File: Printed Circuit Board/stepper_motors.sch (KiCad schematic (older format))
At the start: 8 parts, among them J7 Conn_01x04_Male, J8 Conn_01x04_Male

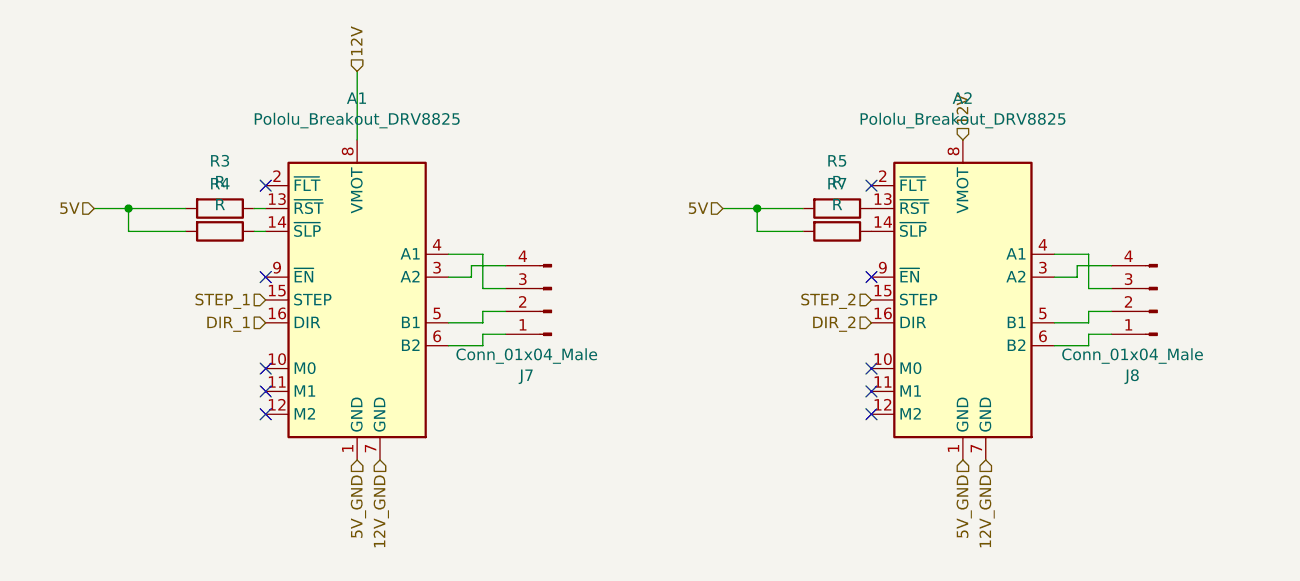
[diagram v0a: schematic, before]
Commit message: PCB: using m0, m1, m2 in stepper motors
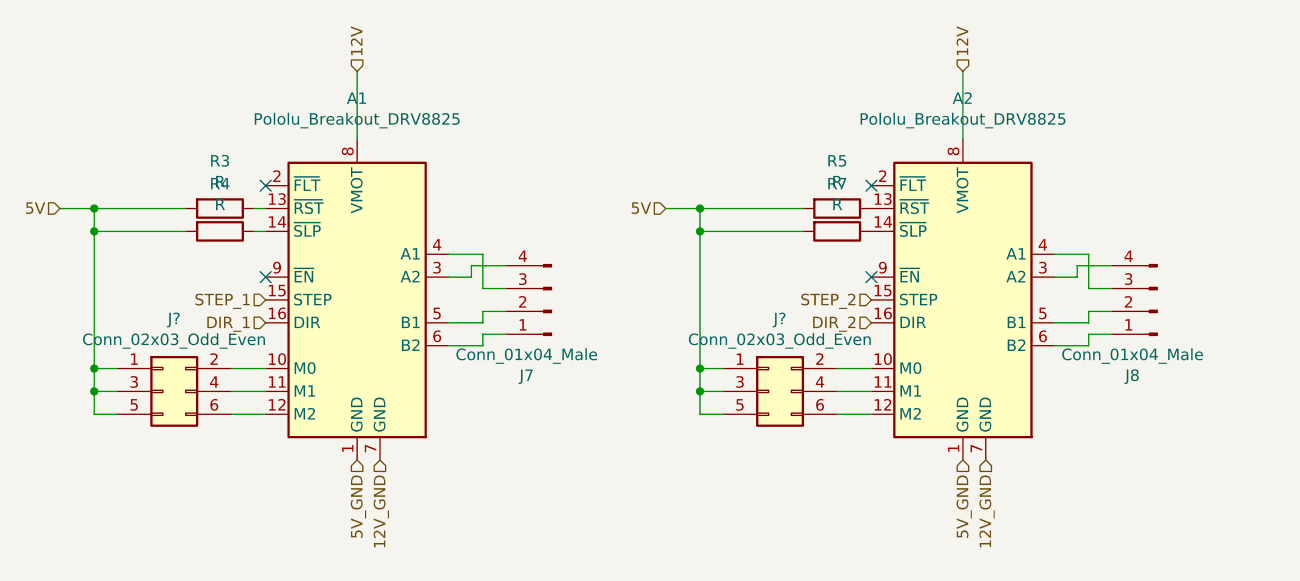
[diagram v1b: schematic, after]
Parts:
- added J? (x2): Conn_02x03_Odd_Even, symbol Connector_Generic:Conn_02x03_Odd_Even
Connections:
- net 5V: now also J?.1 (Pin_1), J?.1 (Pin_1), J?.3 (Pin_3), J?.3 (Pin_3), J?.5 (Pin_5), J?.5 (Pin_5)
- net at A1.10 (M0): now also J?.2 (Pin_2)
- net at A1.11 (M1): now also J?.4 (Pin_4)
- net at A1.12 (M2): now also J?.6 (Pin_6)
- net at A2.10 (M0): now also J?.2 (Pin_2)
- net at A2.11 (M1): now also J?.4 (Pin_4)
- net at A2.12 (M2): now also J?.6 (Pin_6)
- no-connect marks 10 -> 4
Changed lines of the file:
@@
 NoConn ~ 4300 4250
 NoConn ~ 6950 4250
-NoConn ~ 4300 4850
-NoConn ~ 4300 4750
-NoConn ~ 4300 4650
-NoConn ~ 6950 4850
-NoConn ~ 6950 4750
-NoConn ~ 6950 4650
 NoConn ~ 4300 3850
 NoConn ~ 6950 3850
@@
 $Comp
 L Driver_Motor:Pololu_Breakout_DRV8825 A?
-U 1 1 603C24B3
-P 4700 4250
-AR Path="/603C24B3" Ref="A?"  Part="1"
-AR Path="/603B418F/603C24B3" Ref="A1"  Part="1"
-F 0 "A1" H 4700 5031 50  0000 C CNN
-F 1 "Pololu_Breakout_DRV8825" H 4700 4940 50  0000 C CNN
-F 2 "Module:Pololu_Breakout-16_15.2x20.3mm" H 4900 3450 50  0001 L CNN
-F 3 "https://www.pololu.com/product/2982" H 4800 3950 50  0001 C CNN
-	1    4700 4250
-	1    0    0    -1
-$EndComp
-$Comp
-L Driver_Motor:Pololu_Breakout_DRV8825 A?
 U 1 1 603C24C6
 P 7350 4250
@@
 Text HLabel 4700 3350 1    50   Input ~ 0
 12V
-Text HLabel 7350 3650 1    50   Input ~ 0
+Text HLabel 7350 3350 1    50   Input ~ 0
 12V
 Wire Wire Line
-	6300 3950 6450 3950
-Wire Wire Line
-	6650 4050 6450 4050
-Wire Wire Line
-	6450 4050 6450 3950
-Connection ~ 6450 3950
-Wire Wire Line
-	6450 3950 6650 3950
-Text HLabel 6300 3950 0    50   Input ~ 0
+	6050 3950 6200 3950
+Text HLabel 6050 3950 0    50   Input ~ 0
 5V
 $Comp
@@
 	4250 3950 4300 3950
 Wire Wire Line
-	3700 4050 3700 3950
-Wire Wire Line
-	3700 4050 3950 4050
-Connection ~ 3700 3950
-Wire Wire Line
-	3700 3950 3950 3950
-Wire Wire Line
-	3550 3950 3700 3950
-Text HLabel 3550 3950 0    50   Input ~ 0
+	3400 3950 3550 3950
+Text HLabel 3400 3950 0    50   Input ~ 0
 5V
 Text HLabel 7450 5050 3    50   Input ~ 0
@@
 Text HLabel 4300 4450 0    50   Input ~ 0
 DIR_1
+$Comp
+L Connector_Generic:Conn_02x03_Odd_Even J?
+U 1 1 6031900F
+P 6500 4750
+F 0 "J?" H 6550 5067 50  0000 C CNN
+F 1 "Conn_02x03_Odd_Even" H 6550 4976 50  0000 C CNN
+F 2 "" H 6500 4750 50  0001 C CNN
+F 3 "~" H 6500 4750 50  0001 C CNN
+	1    6500 4750
+	1    0    0    -1
+$EndComp
+Wire Wire Line
+	6800 4650 6950 4650
+Wire Wire Line
+	6800 4750 6950 4750
+Wire Wire Line
+	6950 4850 6800 4850
+Wire Wire Line
+	6300 4650 6200 4650
+Wire Wire Line
+	6200 4650 6200 4050
+Connection ~ 6200 3950
+Connection ~ 6200 4050
+Wire Wire Line
+	6200 4050 6200 3950
+Wire Wire Line
+	6200 4050 6650 4050
+Wire Wire Line
+	6200 3950 6650 3950
+Wire Wire Line
+	6200 4650 6200 4750
+Wire Wire Line
+	6200 4750 6300 4750
+Connection ~ 6200 4650
+Wire Wire Line
+	6200 4750 6200 4850
+Wire Wire Line
+	6200 4850 6300 4850
+Connection ~ 6200 4750
+$Comp
+L Connector_Generic:Conn_02x03_Odd_Even J?
+U 1 1 60322CE9
+P 3850 4750
+F 0 "J?" H 3900 5067 50  0000 C CNN
+F 1 "Conn_02x03_Odd_Even" H 3900 4976 50  0000 C CNN
+F 2 "" H 3850 4750 50  0001 C CNN
+F 3 "~" H 3850 4750 50  0001 C CNN
+	1    3850 4750
+	1    0    0    -1
+$EndComp
+Wire Wire Line
+	4150 4650 4300 4650
+Wire Wire Line
+	4150 4750 4300 4750
+Wire Wire Line
+	4300 4850 4150 4850
+Wire Wire Line
+	3650 4650 3550 4650
+Wire Wire Line
+	3550 4650 3550 4750
+Wire Wire Line
+	3550 4750 3650 4750
+Connection ~ 3550 4650
+Wire Wire Line
+	3550 4750 3550 4850
+Wire Wire Line
+	3550 4850 3650 4850
+Connection ~ 3550 4750
+$Comp
+L Driver_Motor:Pololu_Breakout_DRV8825 A?
+U 1 1 603C24B3
+P 4700 4250
+AR Path="/603C24B3" Ref="A?"  Part="1"
+AR Path="/603B418F/603C24B3" Ref="A1"  Part="1"
+F 0 "A1" H 4700 5031 50  0000 C CNN
+F 1 "Pololu_Breakout_DRV8825" H 4700 4940 50  0000 C CNN
+F 2 "Module:Pololu_Breakout-16_15.2x20.3mm" H 4900 3450 50  0001 L CNN
+F 3 "https://www.pololu.com/product/2982" H 4800 3950 50  0001 C CNN
+	1    4700 4250
+	1    0    0    -1
+$EndComp
+Connection ~ 3550 3950
+Wire Wire Line
+	3550 3950 3950 3950
+Wire Wire Line
+	3550 3950 3550 4050
+Wire Wire Line
+	7350 3350 7350 3650
+Wire Wire Line
+	3550 4050 3950 4050
+Connection ~ 3550 4050
+Wire Wire Line
+	3550 4050 3550 4650
 $EndSCHEMATC

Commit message: PCB: physical board prototype
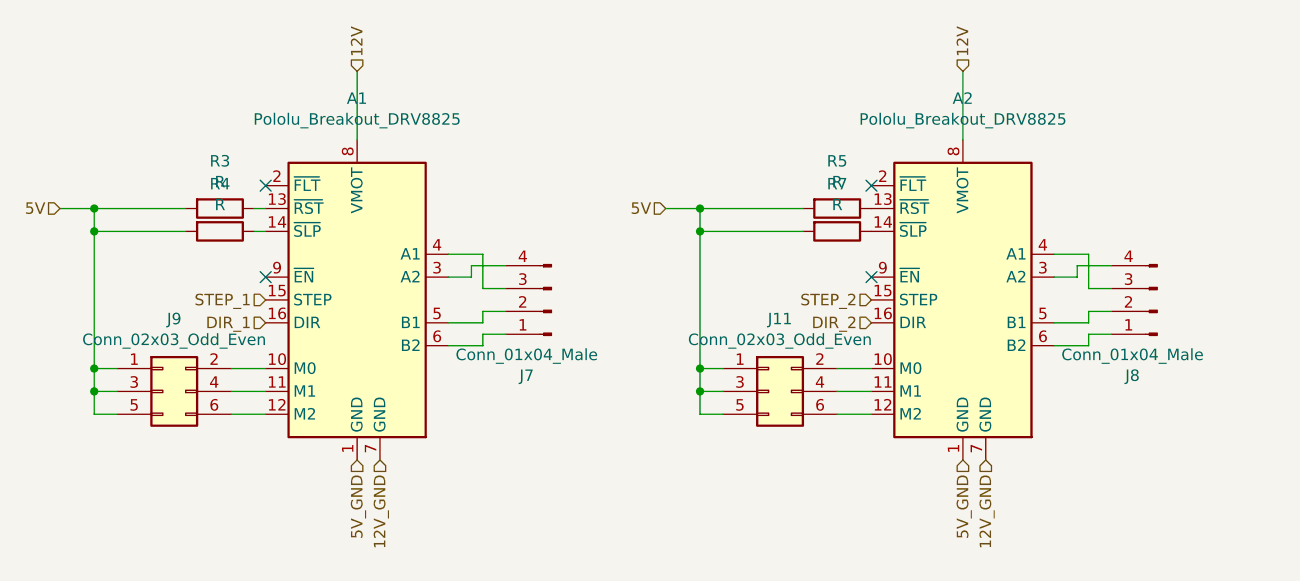
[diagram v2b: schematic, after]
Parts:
- J11: renamed from J?; footprint (none) -> Connector_PinSocket_2.54mm:PinSocket_2x03_P2.54mm_Vertical
- J7, J8: footprint (none) -> Connector_PinHeader_2.54mm:PinHeader_1x04_P2.54mm_Vertical
- J9: renamed from J?; footprint (none) -> Connector_PinSocket_2.54mm:PinSocket_2x03_P2.54mm_Horizontal
- R3, R4, R5, R7: footprint (none) -> Resistor_SMD:R_1206_3216Metric
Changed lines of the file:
@@
 F 0 "J8" H 8308 4681 50  0000 C CNN
 F 1 "Conn_01x04_Male" H 8308 4590 50  0000 C CNN
-F 2 "" H 8200 4400 50  0001 C CNN
+F 2 "Connector_PinHeader_2.54mm:PinHeader_1x04_P2.54mm_Vertical" H 8200 4400 50  0001 C CNN
 F 3 "~" H 8200 4400 50  0001 C CNN
 	1    8200 4400
@@
 F 0 "J7" H 5658 4681 50  0000 C CNN
 F 1 "Conn_01x04_Male" H 5658 4590 50  0000 C CNN
-F 2 "" H 5550 4400 50  0001 C CNN
+F 2 "Connector_PinHeader_2.54mm:PinHeader_1x04_P2.54mm_Vertical" H 5550 4400 50  0001 C CNN
 F 3 "~" H 5550 4400 50  0001 C CNN
 	1    5550 4400
@@
 F 0 "R5" V 6593 3950 50  0000 C CNN
 F 1 "R" V 6684 3950 50  0000 C CNN
-F 2 "" V 6730 3950 50  0001 C CNN
+F 2 "Resistor_SMD:R_1206_3216Metric" V 6730 3950 50  0001 C CNN
 F 3 "~" H 6800 3950 50  0001 C CNN
 	1    6800 3950
@@
 F 0 "R7" V 6593 4050 50  0000 C CNN
 F 1 "R" V 6684 4050 50  0000 C CNN
-F 2 "" V 6730 4050 50  0001 C CNN
+F 2 "Resistor_SMD:R_1206_3216Metric" V 6730 4050 50  0001 C CNN
 F 3 "~" H 6800 4050 50  0001 C CNN
 	1    6800 4050
@@
 F 0 "R4" V 3893 4050 50  0000 C CNN
 F 1 "R" V 3984 4050 50  0000 C CNN
-F 2 "" V 4030 4050 50  0001 C CNN
+F 2 "Resistor_SMD:R_1206_3216Metric" V 4030 4050 50  0001 C CNN
 F 3 "~" H 4100 4050 50  0001 C CNN
 	1    4100 4050
@@
 F 0 "R3" V 3893 3950 50  0000 C CNN
 F 1 "R" V 3984 3950 50  0000 C CNN
-F 2 "" V 4030 3950 50  0001 C CNN
+F 2 "Resistor_SMD:R_1206_3216Metric" V 4030 3950 50  0001 C CNN
 F 3 "~" H 4100 3950 50  0001 C CNN
 	1    4100 3950
@@
 DIR_1
 $Comp
-L Connector_Generic:Conn_02x03_Odd_Even J?
+L Connector_Generic:Conn_02x03_Odd_Even J11
 U 1 1 6031900F
 P 6500 4750
-F 0 "J?" H 6550 5067 50  0000 C CNN
+F 0 "J11" H 6550 5067 50  0000 C CNN
 F 1 "Conn_02x03_Odd_Even" H 6550 4976 50  0000 C CNN
-F 2 "" H 6500 4750 50  0001 C CNN
+F 2 "Connector_PinSocket_2.54mm:PinSocket_2x03_P2.54mm_Vertical" H 6500 4750 50  0001 C CNN
 F 3 "~" H 6500 4750 50  0001 C CNN
 	1    6500 4750
@@
 Connection ~ 6200 4750
 $Comp
-L Connector_Generic:Conn_02x03_Odd_Even J?
+L Connector_Generic:Conn_02x03_Odd_Even J9
 U 1 1 60322CE9
 P 3850 4750
-F 0 "J?" H 3900 5067 50  0000 C CNN
+F 0 "J9" H 3900 5067 50  0000 C CNN
 F 1 "Conn_02x03_Odd_Even" H 3900 4976 50  0000 C CNN
-F 2 "" H 3850 4750 50  0001 C CNN
+F 2 "Connector_PinSocket_2.54mm:PinSocket_2x03_P2.54mm_Horizontal" H 3850 4750 50  0001 C CNN
 F 3 "~" H 3850 4750 50  0001 C CNN
 	1    3850 4750

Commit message: PCB physical board
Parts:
- A1: value Pololu_Breakout_DRV8825 -> stepper driver DRV8825 (1)
- A2: value Pololu_Breakout_DRV8825 -> stepper driver DRV8825 (2)
- J11: value Conn_02x03_Odd_Even -> stepper driver M jumper (2)
- J7: value Conn_01x04_Male -> stepper motor connector (1)
- J8: value Conn_01x04_Male -> stepper motor connector (2)
- J9: value Conn_02x03_Odd_Even -> stepper driver M jumper (1); footprint Connector_PinSocket_2.54mm:PinSocket_2x03_P2.54mm_Horizontal -> Connector_PinSocket_2.54mm:PinSocket_2x03_P2.54mm_Vertical
- R7: value R -> SLP_R_2
- renumbered R3 to RST_R_1, R5 to RST_R_2, R4 to SLP_R_1
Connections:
- net at J11.2 (Pin_2): now also A2.12 (M2); no longer A2.10 (M0)
- net at J11.6 (Pin_6): now also A2.10 (M0); no longer A2.12 (M2)
- net at J9.2 (Pin_2): now also A1.12 (M2); no longer A1.10 (M0)
- net at J9.6 (Pin_6): now also A1.10 (M0); no longer A1.12 (M2)
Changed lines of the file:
@@
 AR Path="/603B418F/603C2499" Ref="J8"  Part="1"
 F 0 "J8" H 8308 4681 50  0000 C CNN
-F 1 "Conn_01x04_Male" H 8308 4590 50  0000 C CNN
+F 1 "stepper motor connector (2)" H 8308 4590 50  0000 C CNN
 F 2 "Connector_PinHeader_2.54mm:PinHeader_1x04_P2.54mm_Vertical" H 8200 4400 50  0001 C CNN
 F 3 "~" H 8200 4400 50  0001 C CNN
@@
 AR Path="/603B418F/603C24AC" Ref="J7"  Part="1"
 F 0 "J7" H 5658 4681 50  0000 C CNN
-F 1 "Conn_01x04_Male" H 5658 4590 50  0000 C CNN
+F 1 "stepper motor connector (1)" H 5658 4590 50  0000 C CNN
 F 2 "Connector_PinHeader_2.54mm:PinHeader_1x04_P2.54mm_Vertical" H 5550 4400 50  0001 C CNN
 F 3 "~" H 5550 4400 50  0001 C CNN
@@
 AR Path="/603B418F/603C24C6" Ref="A2"  Part="1"
 F 0 "A2" H 7350 5031 50  0000 C CNN
-F 1 "Pololu_Breakout_DRV8825" H 7350 4940 50  0000 C CNN
+F 1 "stepper driver DRV8825 (2)" H 7350 4940 50  0000 C CNN
 F 2 "Module:Pololu_Breakout-16_15.2x20.3mm" H 7550 3450 50  0001 L CNN
 F 3 "https://www.pololu.com/product/2982" H 7450 3950 50  0001 C CNN
@@
 P 6800 3950
 AR Path="/603C24CC" Ref="R?"  Part="1"
-AR Path="/603B418F/603C24CC" Ref="R5"  Part="1"
-F 0 "R5" V 6593 3950 50  0000 C CNN
+AR Path="/603B418F/603C24CC" Ref="RST_R_2"  Part="1"
+F 0 "RST_R_2" V 6593 3950 50  0000 C CNN
 F 1 "R" V 6684 3950 50  0000 C CNN
 F 2 "Resistor_SMD:R_1206_3216Metric" V 6730 3950 50  0001 C CNN
@@
 AR Path="/603B418F/603C24D3" Ref="R7"  Part="1"
 F 0 "R7" V 6593 4050 50  0000 C CNN
-F 1 "R" V 6684 4050 50  0000 C CNN
+F 1 "SLP_R_2" V 6684 4050 50  0000 C CNN
 F 2 "Resistor_SMD:R_1206_3216Metric" V 6730 4050 50  0001 C CNN
 F 3 "~" H 6800 4050 50  0001 C CNN
@@
 P 4100 4050
 AR Path="/603D354E" Ref="R?"  Part="1"
-AR Path="/603B418F/603D354E" Ref="R4"  Part="1"
-F 0 "R4" V 3893 4050 50  0000 C CNN
+AR Path="/603B418F/603D354E" Ref="SLP_R_1"  Part="1"
+F 0 "SLP_R_1" V 3893 4050 50  0000 C CNN
 F 1 "R" V 3984 4050 50  0000 C CNN
 F 2 "Resistor_SMD:R_1206_3216Metric" V 4030 4050 50  0001 C CNN
@@
 P 4100 3950
 AR Path="/603D41C9" Ref="R?"  Part="1"
-AR Path="/603B418F/603D41C9" Ref="R3"  Part="1"
-F 0 "R3" V 3893 3950 50  0000 C CNN
+AR Path="/603B418F/603D41C9" Ref="RST_R_1"  Part="1"
+F 0 "RST_R_1" V 3893 3950 50  0000 C CNN
 F 1 "R" V 3984 3950 50  0000 C CNN
 F 2 "Resistor_SMD:R_1206_3216Metric" V 4030 3950 50  0001 C CNN
@@
 P 6500 4750
 F 0 "J11" H 6550 5067 50  0000 C CNN
-F 1 "Conn_02x03_Odd_Even" H 6550 4976 50  0000 C CNN
+F 1 "stepper driver M jumper (2)" H 6550 4976 50  0000 C CNN
 F 2 "Connector_PinSocket_2.54mm:PinSocket_2x03_P2.54mm_Vertical" H 6500 4750 50  0001 C CNN
 F 3 "~" H 6500 4750 50  0001 C CNN
@@
 $EndComp
 Wire Wire Line
-	6800 4650 6950 4650
-Wire Wire Line
 	6800 4750 6950 4750
-Wire Wire Line
-	6950 4850 6800 4850
 Wire Wire Line
 	6300 4650 6200 4650
@@
 P 3850 4750
 F 0 "J9" H 3900 5067 50  0000 C CNN
-F 1 "Conn_02x03_Odd_Even" H 3900 4976 50  0000 C CNN
-F 2 "Connector_PinSocket_2.54mm:PinSocket_2x03_P2.54mm_Horizontal" H 3850 4750 50  0001 C CNN
+F 1 "stepper driver M jumper (1)" H 3900 4976 50  0000 C CNN
+F 2 "Connector_PinSocket_2.54mm:PinSocket_2x03_P2.54mm_Vertical" H 3850 4750 50  0001 C CNN
 F 3 "~" H 3850 4750 50  0001 C CNN
 	1    3850 4750
@@
 $EndComp
 Wire Wire Line
-	4150 4650 4300 4650
-Wire Wire Line
 	4150 4750 4300 4750
-Wire Wire Line
-	4300 4850 4150 4850
 Wire Wire Line
 	3650 4650 3550 4650
@@
 AR Path="/603B418F/603C24B3" Ref="A1"  Part="1"
 F 0 "A1" H 4700 5031 50  0000 C CNN
-F 1 "Pololu_Breakout_DRV8825" H 4700 4940 50  0000 C CNN
+F 1 "stepper driver DRV8825 (1)" H 4700 4940 50  0000 C CNN
 F 2 "Module:Pololu_Breakout-16_15.2x20.3mm" H 4900 3450 50  0001 L CNN
 F 3 "https://www.pololu.com/product/2982" H 4800 3950 50  0001 C CNN
@@
 Wire Wire Line
 	3550 4050 3550 4650
+Wire Wire Line
+	4150 4650 4250 4650
+Wire Wire Line
+	4250 4650 4250 4850
+Wire Wire Line
+	4250 4850 4300 4850
+Wire Wire Line
+	4300 4650 4300 4700
+Wire Wire Line
+	4300 4700 4200 4700
+Wire Wire Line
+	4200 4700 4200 4850
+Wire Wire Line
+	4200 4850 4150 4850
+Wire Wire Line
+	6800 4650 6900 4650
+Wire Wire Line
+	6900 4650 6900 4850
+Wire Wire Line
+	6900 4850 6950 4850
+Wire Wire Line
+	6950 4650 6950 4700
+Wire Wire Line
+	6950 4700 6850 4700
+Wire Wire Line
+	6850 4700 6850 4850
+Wire Wire Line
+	6850 4850 6800 4850
 $EndSCHEMATC
